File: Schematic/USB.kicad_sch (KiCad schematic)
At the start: 5 parts, among them J3 USB_C_Receptacle_USB2.0_14P, U3 USBLC6-2SC6

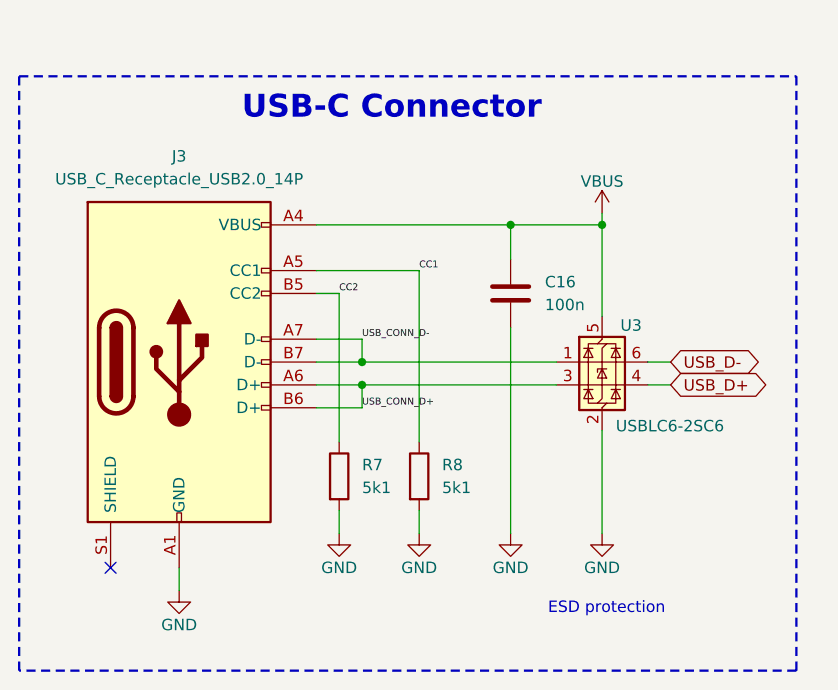
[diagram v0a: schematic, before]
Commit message: Made board smaller
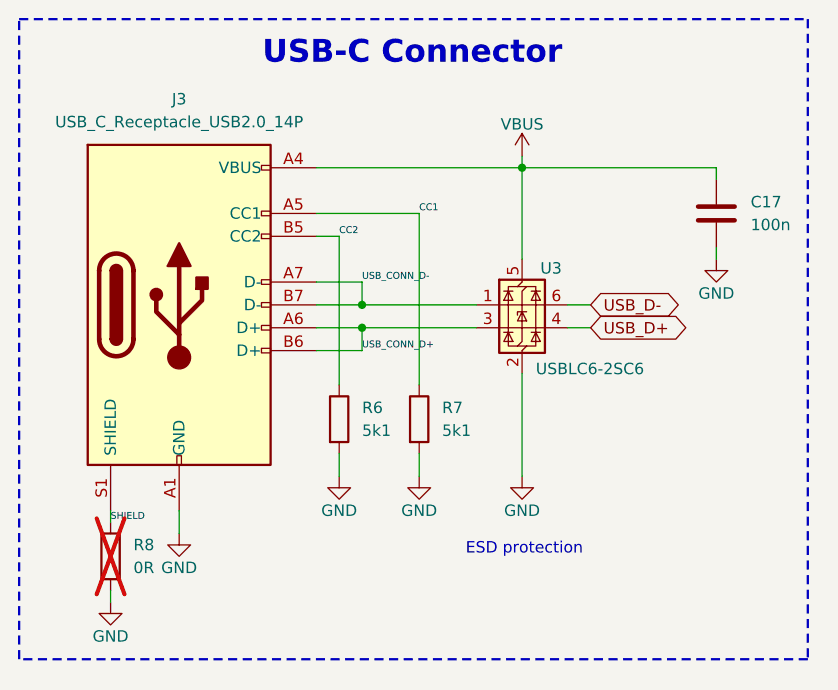
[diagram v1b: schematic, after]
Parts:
- added R8: 0R, Resistor_SMD:R_0805_2012Metric, symbol Device:R
- renumbered C16 to C17, R7 to R6, R8 to R7
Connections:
- net GND: now also R8.2
- net SHIELD: now reaches J3.S1 (SHIELD)
- net SHIELD: now also R8.1
- no-connect marks 1 -> 0
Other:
- moved on the sheet: C17, J3, R6, R7, U3

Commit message: V1.0
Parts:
- renumbered C17 to C16, J3 to J2, R6 to R10, R7 to R11, R8 to R12
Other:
- moved on the sheet: C16
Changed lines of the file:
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@@
 	(title_block
 		(title "Icarus Flight Computer")
-		(date "2025-04-30")
+		(date "2025-05-20")
 		(rev "V1.0")
 		(company "Daedalus Industries")
-		(comment 1 "Onboard flight computer for the Icarus rocket")
+		(comment 1 "Onboard flight computer for the rocket \"Icarus\"")
 		(comment 2 "USB-C connector for power and debug")
 		(comment 3 "Designer: Mattia Gregnanin")
@@
 	(rectangle
 		(start 64.77 25.4)
-		(end 152.4 96.52)
+		(end 153.67 96.52)
 		(stroke
 			(width 0.254)
@@
 	(text "USB-C Connector"
 		(exclude_from_sim no)
-		(at 108.458 29.21 0)
+		(at 109.22 29.21 0)
 		(effects
 			(font
@@
 	(wire
 		(pts
-			(xy 142.24 52.07) (xy 142.24 50.8)
-		)
-		(stroke
-			(width 0)
-			(type default)
-		)
-	)
-	(wire
-		(pts
-			(xy 120.65 41.91) (xy 142.24 41.91)
-		)
-		(stroke
-			(width 0)
-			(type default)
-		)
-	)
-	(wire
-		(pts
-			(xy 142.24 41.91) (xy 142.24 43.18)
+			(xy 143.51 76.2) (xy 143.51 62.23)
+		)
+		(stroke
+			(width 0)
+			(type default)
+		)
+	)
+	(wire
+		(pts
+			(xy 120.65 41.91) (xy 143.51 41.91)
+		)
+		(stroke
+			(width 0)
+			(type default)
+		)
+	)
+	(wire
+		(pts
+			(xy 143.51 41.91) (xy 143.51 54.61)
 		)
 		(stroke
@@
 		(dnp yes)
 		(fields_autoplaced yes)
-		(property "Reference" "R8"
+		(property "Reference" "R12"
 			(at 77.47 83.8199 0)
 			(effects
@@
 			(project ""
 				(path "/2a10c6de-1617-4216-ace2-cdde3ce2909e/9335a33c-17b0-4aec-be7f-6e8ea11dab08"
-					(reference "R8")
+					(reference "R12")
 					(unit 1)
 				)
@@
 		(dnp no)
 		(fields_autoplaced yes)
-		(property "Reference" "J3"
+		(property "Reference" "J2"
 			(at 82.55 34.29 0)
 			(effects
@@
 			(project ""
 				(path "/2a10c6de-1617-4216-ace2-cdde3ce2909e/9335a33c-17b0-4aec-be7f-6e8ea11dab08"
-					(reference "J3")
+					(reference "J2")
 					(unit 1)
 				)
@@
 	(symbol
 		(lib_id "power:GND")
-		(at 142.24 52.07 0)
+		(at 143.51 76.2 0)
 		(unit 1)
 		(exclude_from_sim no)
@@
 		(dnp no)
 		(property "Reference" "#PWR035"
-			(at 142.24 58.42 0)
+			(at 143.51 82.55 0)
 			(effects
 				(font
@@
 		)
 		(property "Value" "GND"
-			(at 142.24 55.88 0)
+			(at 143.51 80.01 0)
 			(effects
 				(font
@@
 		)
 		(property "Footprint" ""
-			(at 142.24 52.07 0)
+			(at 143.51 76.2 0)
 			(effects
 				(font
@@
 		)
 		(property "Datasheet" ""
-			(at 142.24 52.07 0)
+			(at 143.51 76.2 0)
 			(effects
 				(font
@@
 		)
 		(property "Description" "Power symbol creates a global label with name \"GND\" , ground"
-			(at 142.24 52.07 0)
+			(at 143.51 76.2 0)
 			(effects
 				(font
@@
 		(dnp no)
 		(fields_autoplaced yes)
-		(property "Reference" "R6"
+		(property "Reference" "R10"
 			(at 102.87 68.5799 0)
 			(effects
@@
 			(project ""
 				(path "/2a10c6de-1617-4216-ace2-cdde3ce2909e/9335a33c-17b0-4aec-be7f-6e8ea11dab08"
-					(reference "R6")
+					(reference "R10")
 					(unit 1)
 				)
@@
 		(dnp no)
 		(fields_autoplaced yes)
-		(property "Reference" "R7"
+		(property "Reference" "R11"
 			(at 111.76 68.5799 0)
 			(effects
@@
 			(project "Icarus Flight Computer"
 				(path "/2a10c6de-1617-4216-ace2-cdde3ce2909e/9335a33c-17b0-4aec-be7f-6e8ea11dab08"
-					(reference "R7")
+					(reference "R11")
 					(unit 1)
 				)
@@
 	(symbol
 		(lib_id "Device:C")
-		(at 142.24 46.99 0)
+		(at 143.51 58.42 0)
 		(unit 1)
 		(exclude_from_sim no)
@@
 		(dnp no)
 		(fields_autoplaced yes)
-		(property "Reference" "C17"
-			(at 146.05 45.7199 0)
+		(property "Reference" "C16"
+			(at 147.32 57.1499 0)
 			(effects
 				(font
@@
 		)
 		(property "Value" "100n"
-			(at 146.05 48.2599 0)
+			(at 147.32 59.6899 0)
 			(effects
 				(font
@@
 		)
 		(property "Footprint" "Capacitor_SMD:C_0402_1005Metric"
-			(at 143.2052 50.8 0)
+			(at 144.4752 62.23 0)
 			(effects
 				(font
@@
 		)
 		(property "Datasheet" "~"
-			(at 142.24 46.99 0)
+			(at 143.51 58.42 0)
 			(effects
 				(font
@@
 		)
 		(property "Description" "Unpolarized capacitor"
-			(at 142.24 46.99 0)
+			(at 143.51 58.42 0)
 			(effects
 				(font
@@
 		)
 		(property "MPN" "C1525"
-			(at 142.24 46.99 0)
+			(at 143.51 58.42 0)
 			(effects
 				(font
@@
 			(project "Icarus Flight Computer"
 				(path "/2a10c6de-1617-4216-ace2-cdde3ce2909e/9335a33c-17b0-4aec-be7f-6e8ea11dab08"
-					(reference "C17")
+					(reference "C16")
 					(unit 1)
 				)
